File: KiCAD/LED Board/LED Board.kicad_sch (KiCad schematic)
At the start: 11 parts, among them J1 Conn_01x03_Socket, J10 Conn_01x03_Socket, J2 Conn_01x03_Socket, J3 Conn_01x03_Socket, J4 Conn_01x03_Socket, J5 Conn_01x03_Socket, J6 Conn_01x03_Socket, J7 Conn_01x03_Socket, J8 Conn_01x03_Socket, J9 Conn_01x03_Socket

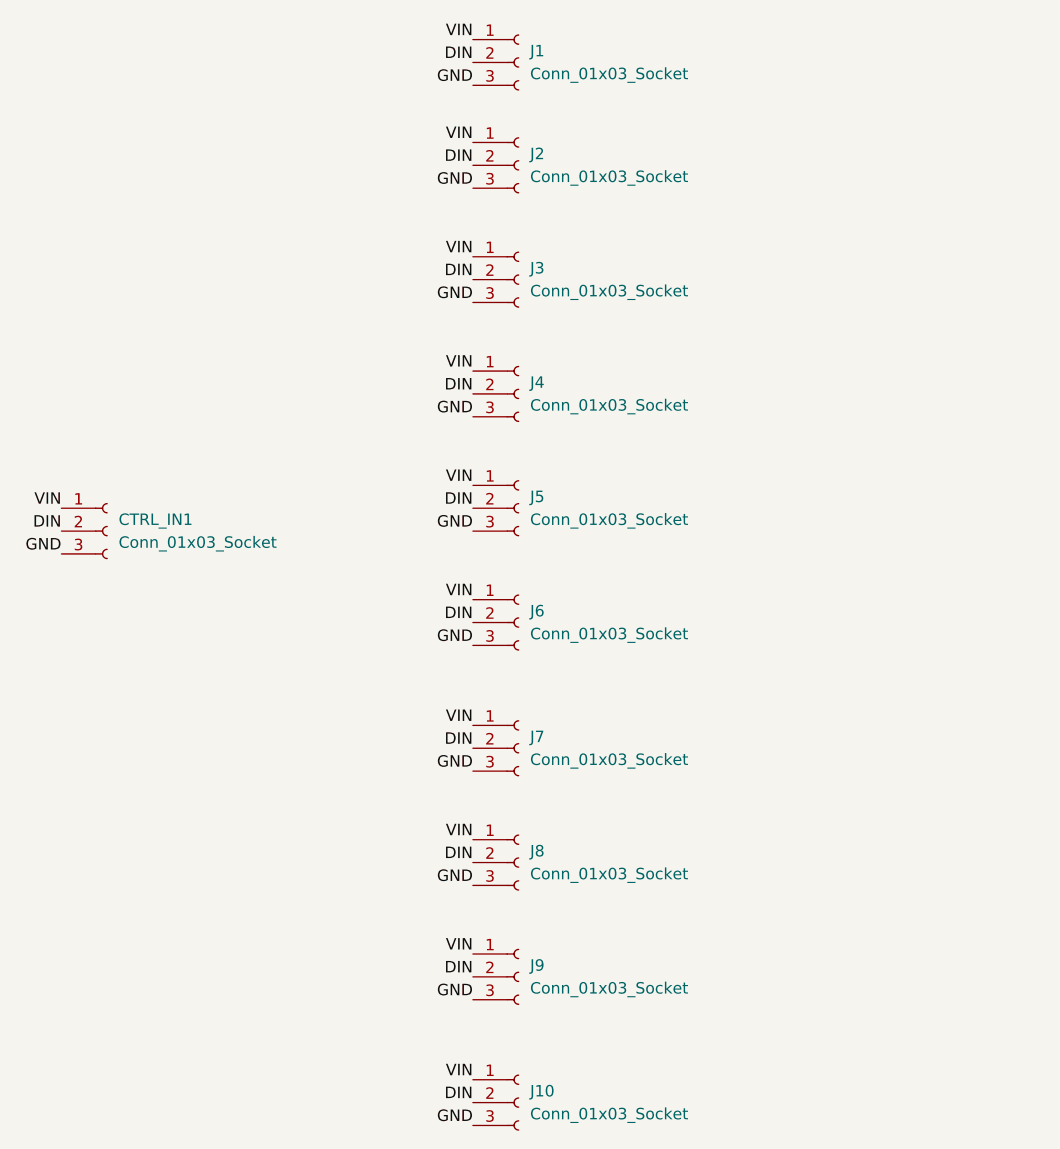
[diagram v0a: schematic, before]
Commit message: Updated LED Socket Board
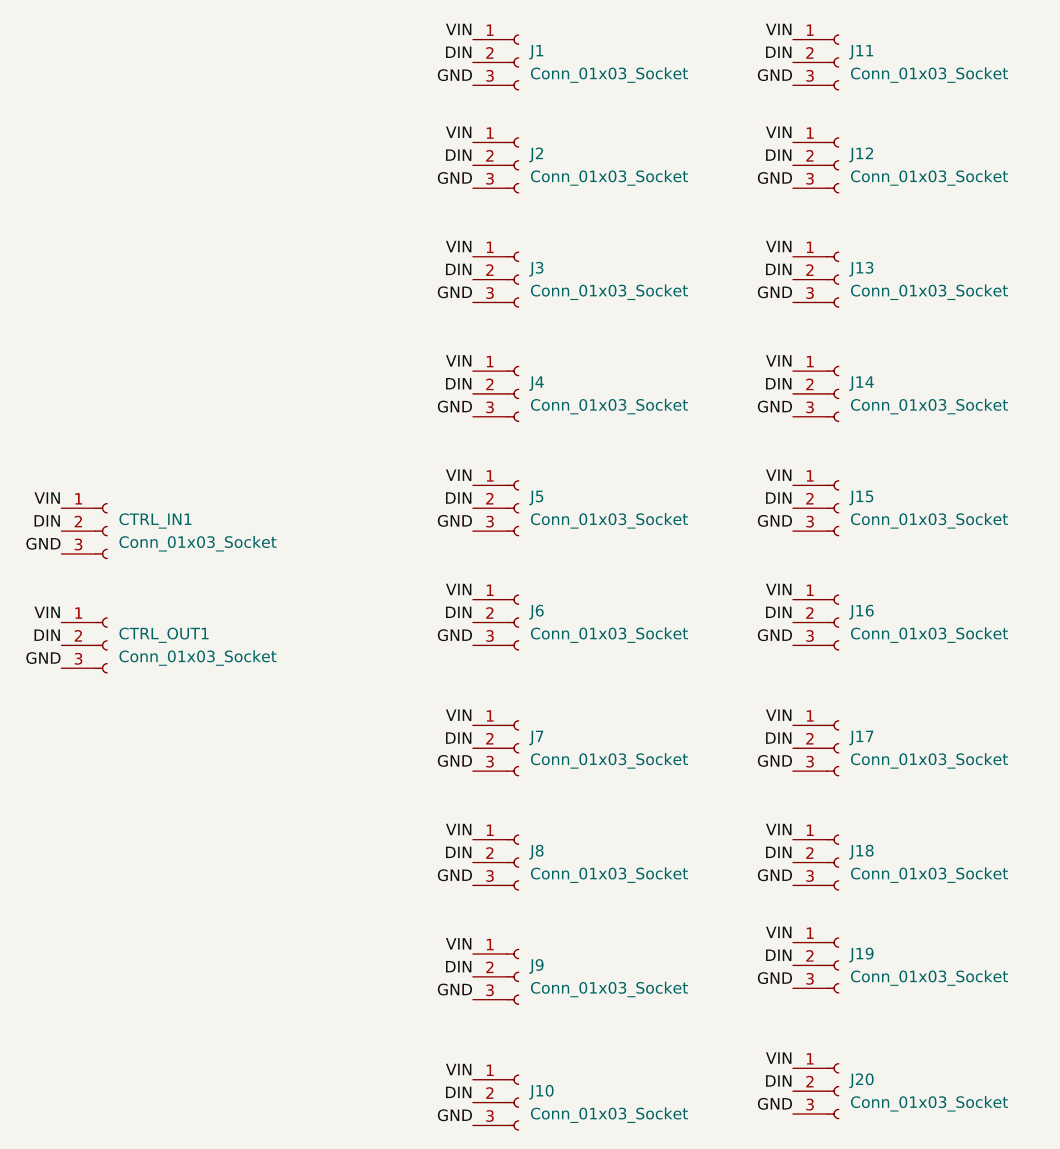
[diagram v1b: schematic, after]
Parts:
- added CTRL_OUT1, J11, J12, J13, J14, J15, J16, J17, J18, J19, J20: Conn_01x03_Socket, CustomConnectorPinSocket2.54mm1x03_Vertical:PinSocket_1x03_P2.54mm_Vertical_HandSolder, symbol Connector:Conn_01x03_Socket
- CTRL_IN1, J1, J10, J2, J3, J4, J5, J6, J7, J8, J9: footprint Connector_PinSocket_2.54mm:PinSocket_1x03_P2.54mm_Vertical -> CustomConnectorPinSocket2.54mm1x03_Vertical:PinSocket_1x03_P2.54mm_Vertical_HandSolder
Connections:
- net DIN: now also CTRL_OUT1.2 (Pin_2), J11.2 (Pin_2), J12.2 (Pin_2), J13.2 (Pin_2), J14.2 (Pin_2), J15.2 (Pin_2), J16.2 (Pin_2), J17.2 (Pin_2), J18.2 (Pin_2), J19.2 (Pin_2), J20.2 (Pin_2)
- net GND: now also CTRL_OUT1.3 (Pin_3), J11.3 (Pin_3), J12.3 (Pin_3), J13.3 (Pin_3), J14.3 (Pin_3), J15.3 (Pin_3), J16.3 (Pin_3), J17.3 (Pin_3), J18.3 (Pin_3), J19.3 (Pin_3), J20.3 (Pin_3)
- net VIN: now also CTRL_OUT1.1 (Pin_1), J11.1 (Pin_1), J12.1 (Pin_1), J13.1 (Pin_1), J14.1 (Pin_1), J15.1 (Pin_1), J16.1 (Pin_1), J17.1 (Pin_1), J18.1 (Pin_1), J19.1 (Pin_1), J20.1 (Pin_1)
